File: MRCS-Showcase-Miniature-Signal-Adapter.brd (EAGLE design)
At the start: 106 x 100 mm, 4 parts

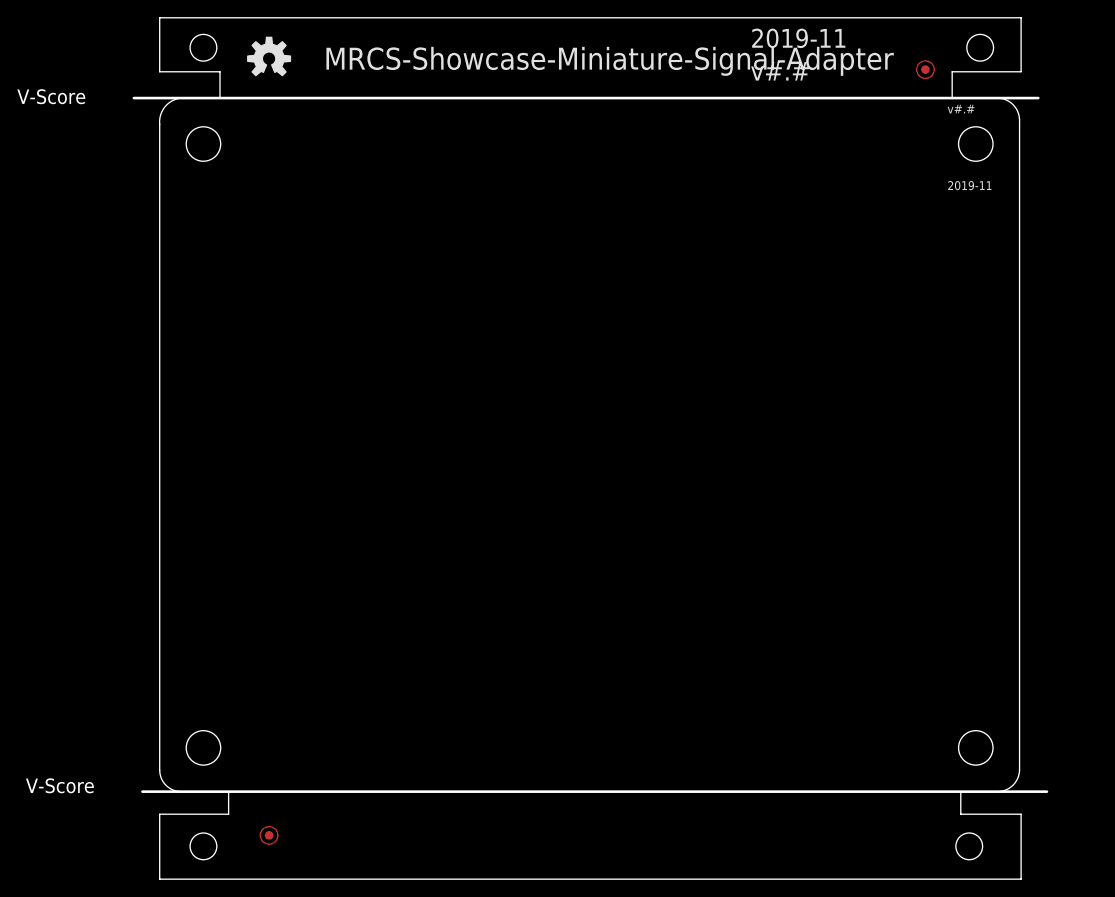
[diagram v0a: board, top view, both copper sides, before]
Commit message: Various adjustments of hole and chip sizes
- changed SMD resistors to 1206 to allow easier soldering
- Changed size of shaft hole to match #52 drill
- changes pads to .6mm for better fit with #24 wire
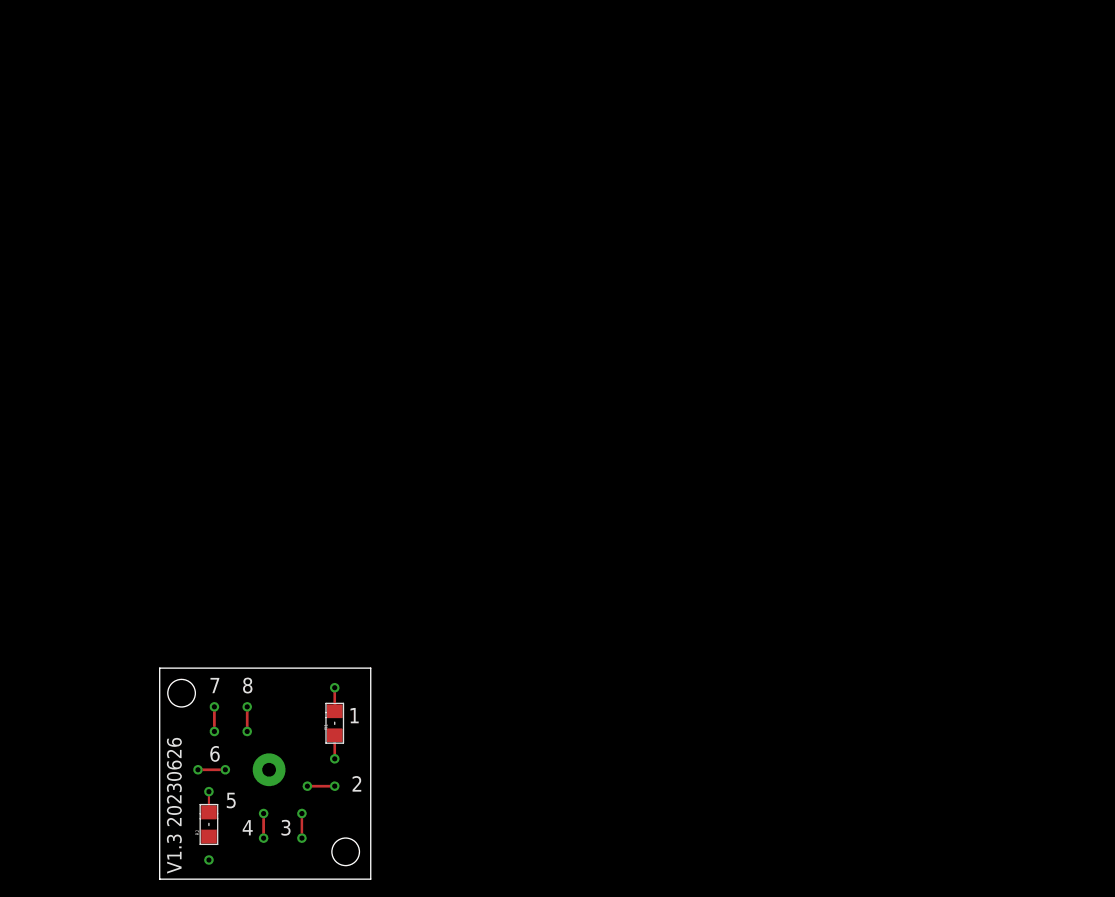
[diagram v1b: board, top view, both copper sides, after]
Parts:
- removed BOARD1: BOARD80X100, SPCoast:BOARD-DINRAIL-3.17INX10CM
- removed FID1, FID2: FIDUCIAL, SPCoast:FIDUCIAL_1MM
- removed OSHW1: DOC-OSHW-LOGO-M, SPCoast:OSHW-LOGO-M
- added R1, R2: 1K, SPCoast:1206-RES
- added TP1, TP10, TP11, TP12, TP13, TP14, TP15, TP16, TP2, TP3, TP4, TP5, TP6, TP7, TP8, TP9: TP, MRCS:P1-06
- added U$1: (no value), MRCSLogoTop:MRCSLOGOTOP
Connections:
- new net N$10: TP16.P$1, TP8.P$1
- new net N$17: R1.2, TP9.P$1
- new net N$2: R1.1, TP1.P$1
- new net N$3: R2.1, TP2.P$1
- new net N$4: R2.2, TP10.P$1
- new net N$5: TP11.P$1, TP3.P$1
- new net N$6: TP12.P$1, TP4.P$1
- new net N$7: TP13.P$1, TP5.P$1
- new net N$8: TP14.P$1, TP6.P$1
- new net N$9: TP15.P$1, TP7.P$1
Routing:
- net N$10: track 0.00 -> 3.18 mm
- net N$8: track 0.00 -> 3.17 mm
- net N$9: track 0.00 -> 2.86 mm
- net N$6: track 0.00 -> 2.86 mm
- net N$7: track 0.00 -> 2.86 mm
- net N$5: track 0.00 -> 2.86 mm
- net N$17: track 0.00 -> 2.73 mm
- net N$2: track 0.00 -> 2.73 mm
- net N$4: track 0.00 -> 2.41 mm
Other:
- board size 106 x 100 mm -> 24.5 x 24.5 mm
- board text added: "1"
- board text added: "2"
- board text added: "3"
- board text added: "4"
- board text added: "5"
- board text added: "6"
- board text added: "7"
- board text added: "8"
- board text added: "V1.3 20230626"
- board text removed: "2019-11"
- board text removed: ">DRAWING_NAME"
- board text removed: "Use tPlace/bPlace for silkscreen text and drawings Use Document, tDocu and bDocu for assembly notes and documentation that does NOT go on the board"
- board text removed: "v#.#"
